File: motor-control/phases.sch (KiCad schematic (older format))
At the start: 39 parts

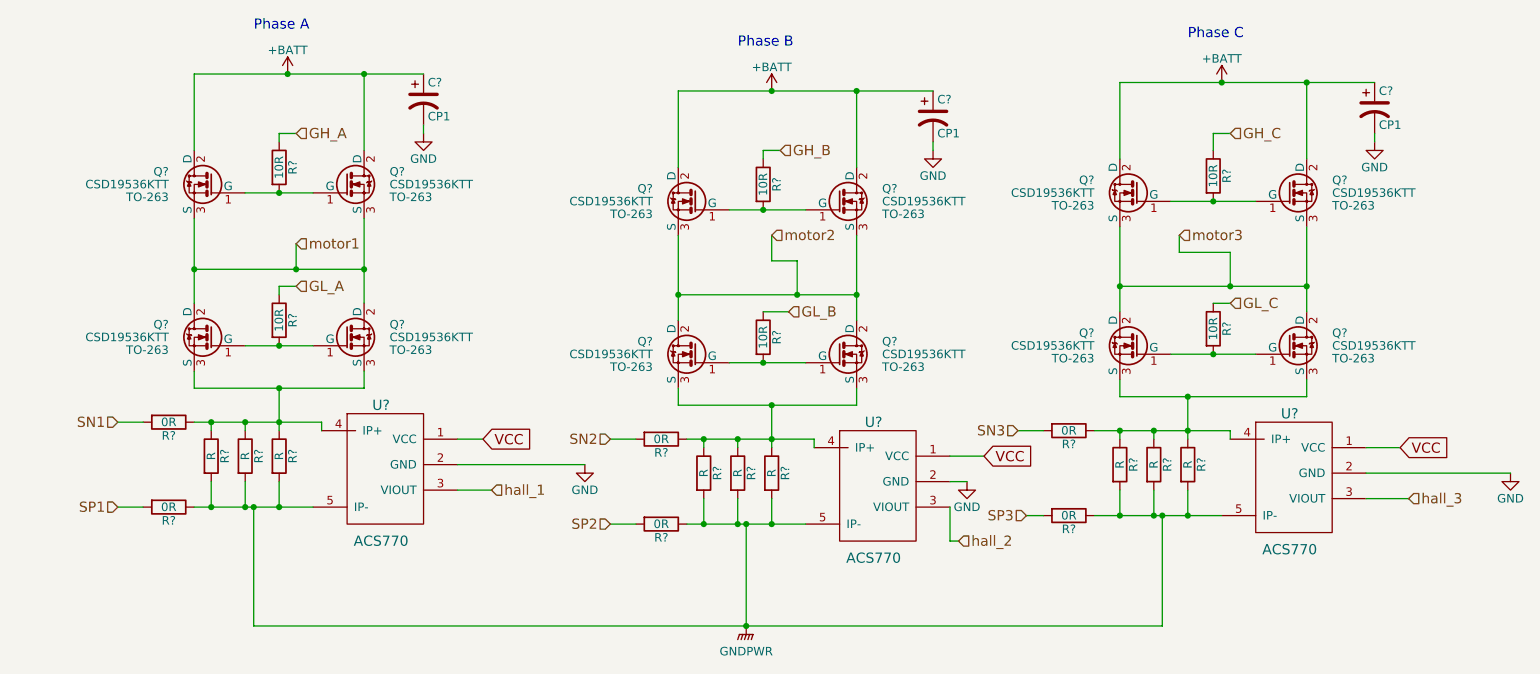
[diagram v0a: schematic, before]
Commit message: Almost finished gate driver schematic
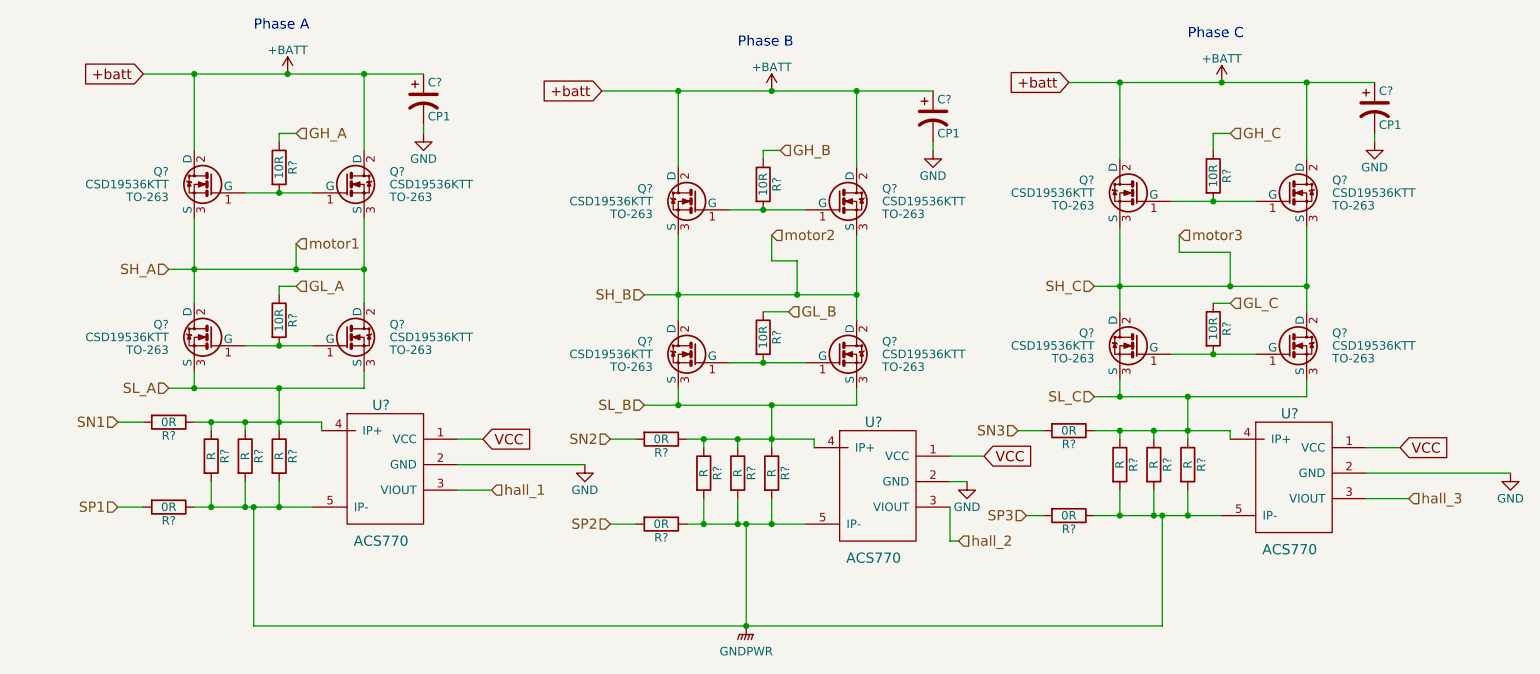
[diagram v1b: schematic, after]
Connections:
- net SL_A: now reaches Q?.3 (S), Q?.3 (S), R?.1, R?.1, R?.1, R?.1, U?.4 (IP+)
- net SL_B: now reaches Q?.3 (S), Q?.3 (S), R?.1, R?.1, R?.1, R?.1, U?.4 (IP+)
- net SL_C: now reaches Q?.3 (S), Q?.3 (S), R?.1, R?.1, R?.1, R?.1, U?.4 (IP+)
- net motor1 renamed SH_A
- net motor2 renamed SH_B
- net motor3 renamed SH_C
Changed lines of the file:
@@
 encoding utf-8
 Sheet 2 3
-Title ""
-Date ""
-Rev ""
-Comp ""
-Comment1 ""
+Title "Power MOSFETs"
+Date "2015-11-18"
+Rev "1"
+Comp "RIT Senior Design"
+Comment1 "Joseph Kubeck"
 Comment2 ""
 Comment3 ""
@@
 	4650 2300 4650 2250
 Wire Wire Line
-	3300 1950 4650 1950
+	3000 1950 4650 1950
 Wire Wire Line
 	4300 1950 4300 2400
@@
 	4300 3800 4300 3700
 Wire Wire Line
-	3300 3800 4300 3800
+	3150 3800 4300 3800
 Wire Wire Line
 	3300 3800 3300 3700
@@
 	3300 2800 3300 3300
 Wire Wire Line
-	3300 3100 4300 3100
+	3150 3100 4300 3100
 Connection ~ 4300 3100
 Connection ~ 3300 3100
@@
 $EndComp
 Wire Wire Line
-	6150 2050 7650 2050
+	5700 2050 7650 2050
 Wire Wire Line
 	7200 2050 7200 2500
@@
 	7200 3900 7200 3800
 Wire Wire Line
-	6150 3900 7200 3900
+	5950 3900 7200 3900
 Wire Wire Line
 	6150 3900 6150 3800
 Connection ~ 6700 3900
 Wire Wire Line
-	6150 3250 7200 3250
+	5950 3250 7200 3250
 Connection ~ 7200 3250
 Connection ~ 6150 3250
@@
 $EndComp
 Wire Wire Line
-	8750 2000 10250 2000
+	8450 2000 10250 2000
 Wire Wire Line
 	9850 2000 9850 2450
@@
 	8750 3750 8750 3850
 Wire Wire Line
-	8750 3850 9850 3850
+	8600 3850 9850 3850
 Wire Wire Line
 	9850 3850 9850 3750
 Wire Wire Line
-	8750 3200 9850 3200
+	8600 3200 9850 3200
 Connection ~ 9850 3200
 Connection ~ 8750 3200
@@
 Connection ~ 3400 4000
 Connection ~ 3400 4500
+Text HLabel 3150 3100 0    60   Input ~ 0
+SH_A
+Text HLabel 3150 3800 0    60   Input ~ 0
+SL_A
+Text HLabel 5950 3250 0    60   Input ~ 0
+SH_B
+Text HLabel 5950 3900 0    60   Input ~ 0
+SL_B
+Text HLabel 8600 3200 0    60   Input ~ 0
+SH_C
+Text HLabel 8600 3850 0    60   Input ~ 0
+SL_C
+Connection ~ 3300 3800
+Connection ~ 6150 3900
+Connection ~ 8750 3850
+Text GLabel 3000 1950 0    60   Input ~ 0
++batt
+Connection ~ 3300 1950
+Text GLabel 5700 2050 0    60   Input ~ 0
++batt
+Text GLabel 8450 2000 0    60   Input ~ 0
++batt
+Connection ~ 6150 2050
+Connection ~ 8750 2000
 $EndSCHEMATC

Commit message: Annotated schematic & matched footprints
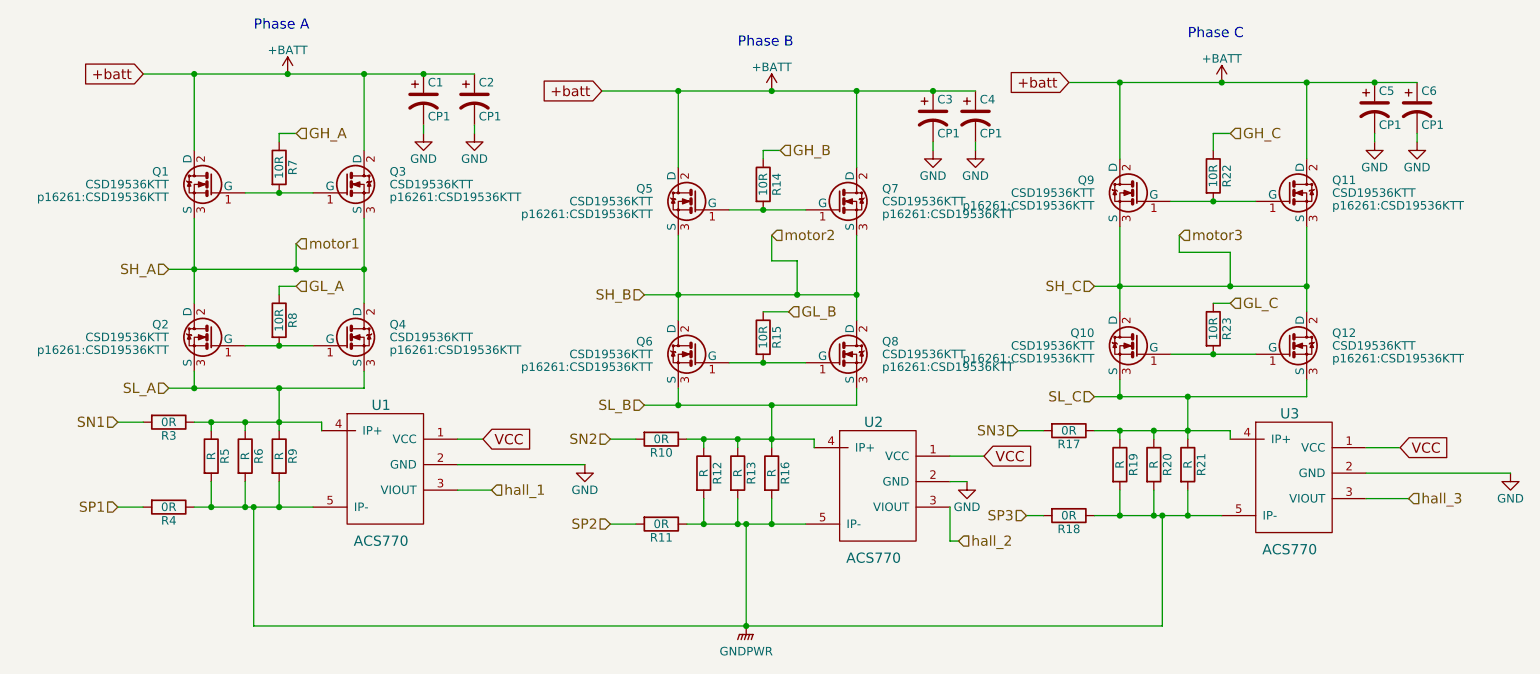
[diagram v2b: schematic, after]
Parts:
- added C2, C4, C6: CP1, Capacitors_Elko_ThroughHole:Elko_vert_31.5x16mm_RM7.5, symbol CP1
- C1, C3, C5: renamed from C?; footprint (none) -> Capacitors_Elko_ThroughHole:Elko_vert_31.5x16mm_RM7.5
- Q1, Q10, Q11, Q12, Q2, Q3, Q4, Q5, Q6, Q7, Q8, Q9: renamed from Q?; footprint TO-263 -> p16261:CSD19536KTT
- R10, R11, R12, R13, R14, R15, R16, R17, R18, R19, R20, R21, R22, R23, R3, R4, R5, R6, R7, R8, R9: renamed from R?; footprint (none) -> Resistors_SMD:R_0805
- U1, U2, U3: renamed from U?; footprint (none) -> p16261:ACS770xCB
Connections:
- net +BATT: now also C2.1, C4.1, C6.1
- net GND: now also C2.2, C4.2, C6.2

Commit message: started revision 2 of board, changed to thru fets
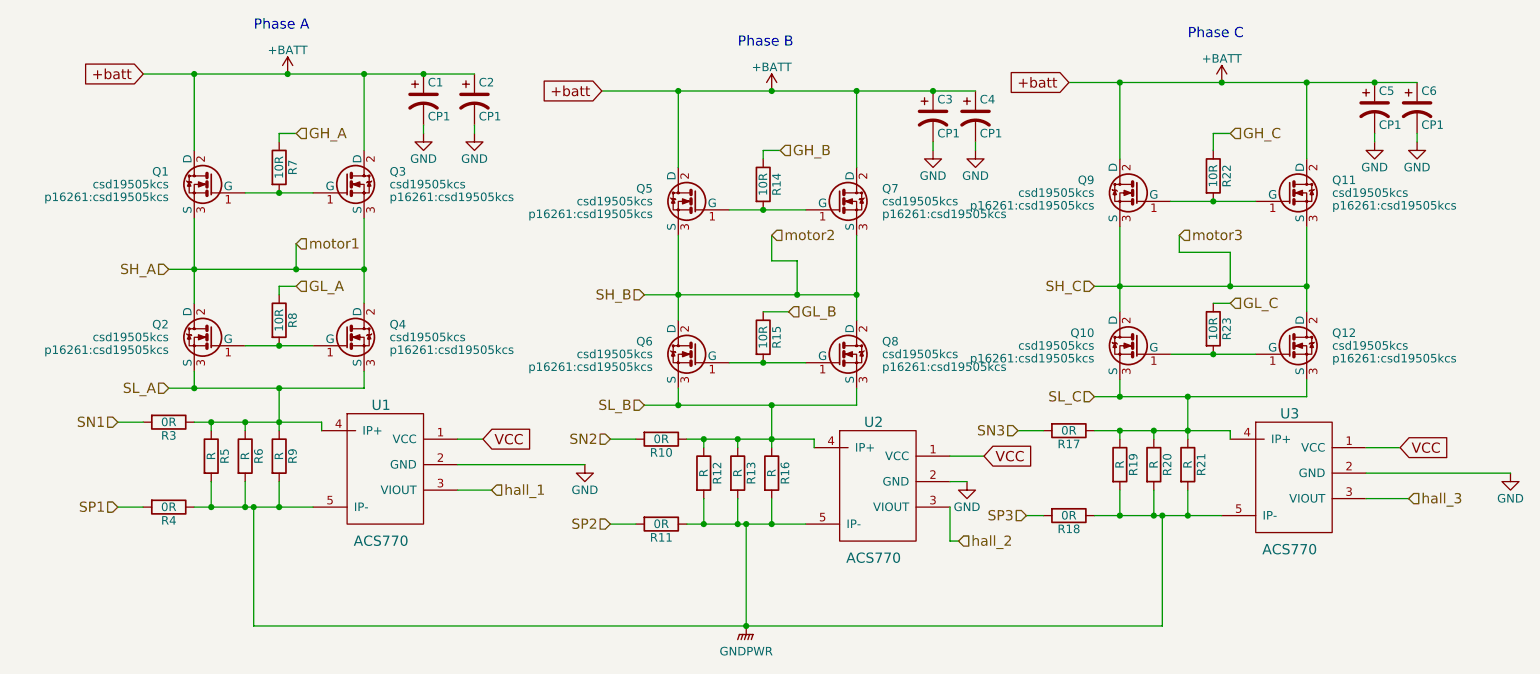
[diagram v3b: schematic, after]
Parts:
- Q1, Q10, Q11, Q12, Q2, Q3, Q4, Q5, Q6, Q7, Q8, Q9: value CSD19536KTT -> csd19505kcs; footprint p16261:CSD19536KTT -> p16261:csd19505kcs
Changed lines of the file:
@@
 P 3400 2600
 F 0 "Q1" H 3650 2675 50  0000 L CNN
-F 1 "CSD19536KTT" H 3650 2600 50  0000 L CNN
-F 2 "p16261:CSD19536KTT" H 3650 2525 50  0000 L CNN
+F 1 "csd19505kcs" H 3650 2600 50  0000 L CNN
+F 2 "p16261:csd19505kcs" H 3650 2525 50  0000 L CNN
 F 3 "" H 3400 2600 50  0000 L CNN
 	1    3400 2600
@@
 P 4200 2600
 F 0 "Q3" H 4450 2675 50  0000 L CNN
-F 1 "CSD19536KTT" H 4450 2600 50  0000 L CNN
-F 2 "p16261:CSD19536KTT" H 4450 2525 50  0000 L CNN
+F 1 "csd19505kcs" H 4450 2600 50  0000 L CNN
+F 2 "p16261:csd19505kcs" H 4450 2525 50  0000 L CNN
 F 3 "" H 4200 2600 50  0000 L CNN
 	1    4200 2600
@@
 P 3400 3500
 F 0 "Q2" H 3650 3575 50  0000 L CNN
-F 1 "CSD19536KTT" H 3650 3500 50  0000 L CNN
-F 2 "p16261:CSD19536KTT" H 3650 3425 50  0000 L CNN
+F 1 "csd19505kcs" H 3650 3500 50  0000 L CNN
+F 2 "p16261:csd19505kcs" H 3650 3425 50  0000 L CNN
 F 3 "" H 3400 3500 50  0000 L CNN
 	1    3400 3500
@@
 P 4200 3500
 F 0 "Q4" H 4450 3575 50  0000 L CNN
-F 1 "CSD19536KTT" H 4450 3500 50  0000 L CNN
-F 2 "p16261:CSD19536KTT" H 4450 3425 50  0000 L CNN
+F 1 "csd19505kcs" H 4450 3500 50  0000 L CNN
+F 2 "p16261:csd19505kcs" H 4450 3425 50  0000 L CNN
 F 3 "" H 4200 3500 50  0000 L CNN
 	1    4200 3500
@@
 P 6250 3600
 F 0 "Q6" H 6500 3675 50  0000 L CNN
-F 1 "CSD19536KTT" H 6500 3600 50  0000 L CNN
-F 2 "p16261:CSD19536KTT" H 6500 3525 50  0000 L CNN
+F 1 "csd19505kcs" H 6500 3600 50  0000 L CNN
+F 2 "p16261:csd19505kcs" H 6500 3525 50  0000 L CNN
 F 3 "" H 6250 3600 50  0000 L CNN
 	1    6250 3600
@@
 P 7100 3600
 F 0 "Q8" H 7350 3675 50  0000 L CNN
-F 1 "CSD19536KTT" H 7350 3600 50  0000 L CNN
-F 2 "p16261:CSD19536KTT" H 7350 3525 50  0000 L CNN
+F 1 "csd19505kcs" H 7350 3600 50  0000 L CNN
+F 2 "p16261:csd19505kcs" H 7350 3525 50  0000 L CNN
 F 3 "" H 7100 3600 50  0000 L CNN
 	1    7100 3600
@@
 P 6250 2700
 F 0 "Q5" H 6500 2775 50  0000 L CNN
-F 1 "CSD19536KTT" H 6500 2700 50  0000 L CNN
-F 2 "p16261:CSD19536KTT" H 6500 2625 50  0000 L CNN
+F 1 "csd19505kcs" H 6500 2700 50  0000 L CNN
+F 2 "p16261:csd19505kcs" H 6500 2625 50  0000 L CNN
 F 3 "" H 6250 2700 50  0000 L CNN
 	1    6250 2700
@@
 P 7100 2700
 F 0 "Q7" H 7350 2775 50  0000 L CNN
-F 1 "CSD19536KTT" H 7350 2700 50  0000 L CNN
-F 2 "p16261:CSD19536KTT" H 7350 2625 50  0000 L CNN
+F 1 "csd19505kcs" H 7350 2700 50  0000 L CNN
+F 2 "p16261:csd19505kcs" H 7350 2625 50  0000 L CNN
 F 3 "" H 7100 2700 50  0000 L CNN
 	1    7100 2700
@@
 P 8850 2650
 F 0 "Q9" H 9100 2725 50  0000 L CNN
-F 1 "CSD19536KTT" H 9100 2650 50  0000 L CNN
-F 2 "p16261:CSD19536KTT" H 9100 2575 50  0000 L CNN
+F 1 "csd19505kcs" H 9100 2650 50  0000 L CNN
+F 2 "p16261:csd19505kcs" H 9100 2575 50  0000 L CNN
 F 3 "" H 8850 2650 50  0000 L CNN
 	1    8850 2650
@@
 P 9750 2650
 F 0 "Q11" H 10000 2725 50  0000 L CNN
-F 1 "CSD19536KTT" H 10000 2650 50  0000 L CNN
-F 2 "p16261:CSD19536KTT" H 10000 2575 50  0000 L CNN
+F 1 "csd19505kcs" H 10000 2650 50  0000 L CNN
+F 2 "p16261:csd19505kcs" H 10000 2575 50  0000 L CNN
 F 3 "" H 9750 2650 50  0000 L CNN
 	1    9750 2650
@@
 P 8850 3550
 F 0 "Q10" H 9100 3625 50  0000 L CNN
-F 1 "CSD19536KTT" H 9100 3550 50  0000 L CNN
-F 2 "p16261:CSD19536KTT" H 9100 3475 50  0000 L CNN
+F 1 "csd19505kcs" H 9100 3550 50  0000 L CNN
+F 2 "p16261:csd19505kcs" H 9100 3475 50  0000 L CNN
 F 3 "" H 8850 3550 50  0000 L CNN
 	1    8850 3550
@@
 P 9750 3550
 F 0 "Q12" H 10000 3625 50  0000 L CNN
-F 1 "CSD19536KTT" H 10000 3550 50  0000 L CNN
-F 2 "p16261:CSD19536KTT" H 10000 3475 50  0000 L CNN
+F 1 "csd19505kcs" H 10000 3550 50  0000 L CNN
+F 2 "p16261:csd19505kcs" H 10000 3475 50  0000 L CNN
 F 3 "" H 9750 3550 50  0000 L CNN
 	1    9750 3550

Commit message: Just trying to get things together
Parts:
- C1, C2, C3, C4, C5, C6: footprint Capacitors_Elko_ThroughHole:Elko_vert_31.5x16mm_RM7.5 -> Capacitors_ThroughHole:C_Radial_D16_L30_P7.5
- R12, R13, R16, R19, R20, R21, R5, R6, R9: footprint Resistors_SMD:R_0805 -> Resistors_ThroughHole:Resistor_Vertical_RM7.5mm
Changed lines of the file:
@@
 F 0 "C1" H 4675 2200 50  0000 L CNN
 F 1 "CP1" H 4675 2000 50  0000 L CNN
-F 2 "Capacitors_Elko_ThroughHole:Elko_vert_31.5x16mm_RM7.5" H 4650 2100 60  0001 C CNN
+F 2 "Capacitors_ThroughHole:C_Radial_D16_L30_P7.5" H 4650 2100 60  0001 C CNN
 F 3 "" H 4650 2100 60  0000 C CNN
 	1    4650 2100
@@
 F 0 "Q1" H 3650 2675 50  0000 L CNN
 F 1 "csd19505kcs" H 3650 2600 50  0000 L CNN
-F 2 "p16261:csd19505kcs" H 3650 2525 50  0000 L CNN
+F 2 "p16261:csd19505kcs" H 3650 2525 50  0001 L CNN
 F 3 "" H 3400 2600 50  0000 L CNN
 	1    3400 2600
@@
 F 0 "Q3" H 4450 2675 50  0000 L CNN
 F 1 "csd19505kcs" H 4450 2600 50  0000 L CNN
-F 2 "p16261:csd19505kcs" H 4450 2525 50  0000 L CNN
+F 2 "p16261:csd19505kcs" H 4450 2525 50  0001 L CNN
 F 3 "" H 4200 2600 50  0000 L CNN
 	1    4200 2600
@@
 F 0 "Q2" H 3650 3575 50  0000 L CNN
 F 1 "csd19505kcs" H 3650 3500 50  0000 L CNN
-F 2 "p16261:csd19505kcs" H 3650 3425 50  0000 L CNN
+F 2 "p16261:csd19505kcs" H 3650 3425 50  0001 L CNN
 F 3 "" H 3400 3500 50  0000 L CNN
 	1    3400 3500
@@
 F 0 "Q4" H 4450 3575 50  0000 L CNN
 F 1 "csd19505kcs" H 4450 3500 50  0000 L CNN
-F 2 "p16261:csd19505kcs" H 4450 3425 50  0000 L CNN
+F 2 "p16261:csd19505kcs" H 4450 3425 50  0001 L CNN
 F 3 "" H 4200 3500 50  0000 L CNN
 	1    4200 3500
@@
 F 0 "R9" V 3880 4200 50  0000 C CNN
 F 1 "R" V 3800 4200 50  0000 C CNN
-F 2 "Resistors_SMD:R_0805" V 3730 4200 30  0001 C CNN
+F 2 "Resistors_ThroughHole:Resistor_Vertical_RM7.5mm" V 3730 4200 30  0001 C CNN
 F 3 "" H 3800 4200 30  0000 C CNN
 	1    3800 4200
@@
 F 0 "R6" V 3680 4200 50  0000 C CNN
 F 1 "R" V 3600 4200 50  0000 C CNN
-F 2 "Resistors_SMD:R_0805" V 3530 4200 30  0001 C CNN
+F 2 "Resistors_ThroughHole:Resistor_Vertical_RM7.5mm" V 3530 4200 30  0001 C CNN
 F 3 "" H 3600 4200 30  0000 C CNN
 	1    3600 4200
@@
 F 0 "R5" V 3480 4200 50  0000 C CNN
 F 1 "R" V 3400 4200 50  0000 C CNN
-F 2 "Resistors_SMD:R_0805" V 3330 4200 30  0001 C CNN
+F 2 "Resistors_ThroughHole:Resistor_Vertical_RM7.5mm" V 3330 4200 30  0001 C CNN
 F 3 "" H 3400 4200 30  0000 C CNN
 	1    3400 4200
@@
 F 0 "C3" H 7675 2300 50  0000 L CNN
 F 1 "CP1" H 7675 2100 50  0000 L CNN
-F 2 "Capacitors_Elko_ThroughHole:Elko_vert_31.5x16mm_RM7.5" H 7650 2200 60  0001 C CNN
+F 2 "Capacitors_ThroughHole:C_Radial_D16_L30_P7.5" H 7650 2200 60  0001 C CNN
 F 3 "" H 7650 2200 60  0000 C CNN
 	1    7650 2200
@@
 F 0 "Q6" H 6500 3675 50  0000 L CNN
 F 1 "csd19505kcs" H 6500 3600 50  0000 L CNN
-F 2 "p16261:csd19505kcs" H 6500 3525 50  0000 L CNN
+F 2 "p16261:csd19505kcs" H 6500 3525 50  0001 L CNN
 F 3 "" H 6250 3600 50  0000 L CNN
 	1    6250 3600
@@
 F 0 "Q8" H 7350 3675 50  0000 L CNN
 F 1 "csd19505kcs" H 7350 3600 50  0000 L CNN
-F 2 "p16261:csd19505kcs" H 7350 3525 50  0000 L CNN
+F 2 "p16261:csd19505kcs" H 7350 3525 50  0001 L CNN
 F 3 "" H 7100 3600 50  0000 L CNN
 	1    7100 3600
@@
 F 0 "Q5" H 6500 2775 50  0000 L CNN
 F 1 "csd19505kcs" H 6500 2700 50  0000 L CNN
-F 2 "p16261:csd19505kcs" H 6500 2625 50  0000 L CNN
+F 2 "p16261:csd19505kcs" H 6500 2625 50  0001 L CNN
 F 3 "" H 6250 2700 50  0000 L CNN
 	1    6250 2700
@@
 F 0 "Q7" H 7350 2775 50  0000 L CNN
 F 1 "csd19505kcs" H 7350 2700 50  0000 L CNN
-F 2 "p16261:csd19505kcs" H 7350 2625 50  0000 L CNN
+F 2 "p16261:csd19505kcs" H 7350 2625 50  0001 L CNN
 F 3 "" H 7100 2700 50  0000 L CNN
 	1    7100 2700
@@
 F 0 "R12" V 6380 4300 50  0000 C CNN
 F 1 "R" V 6300 4300 50  0000 C CNN
-F 2 "Resistors_SMD:R_0805" V 6230 4300 30  0001 C CNN
+F 2 "Resistors_ThroughHole:Resistor_Vertical_RM7.5mm" V 6230 4300 30  0001 C CNN
 F 3 "" H 6300 4300 30  0000 C CNN
 	1    6300 4300
@@
 F 0 "R13" V 6580 4300 50  0000 C CNN
 F 1 "R" V 6500 4300 50  0000 C CNN
-F 2 "Resistors_SMD:R_0805" V 6430 4300 30  0001 C CNN
+F 2 "Resistors_ThroughHole:Resistor_Vertical_RM7.5mm" V 6430 4300 30  0001 C CNN
 F 3 "" H 6500 4300 30  0000 C CNN
 	1    6500 4300
@@
 F 0 "R16" V 6780 4300 50  0000 C CNN
 F 1 "R" V 6700 4300 50  0000 C CNN
-F 2 "Resistors_SMD:R_0805" V 6630 4300 30  0001 C CNN
+F 2 "Resistors_ThroughHole:Resistor_Vertical_RM7.5mm" V 6630 4300 30  0001 C CNN
 F 3 "" H 6700 4300 30  0000 C CNN
 	1    6700 4300
@@
 F 0 "Q9" H 9100 2725 50  0000 L CNN
 F 1 "csd19505kcs" H 9100 2650 50  0000 L CNN
-F 2 "p16261:csd19505kcs" H 9100 2575 50  0000 L CNN
+F 2 "p16261:csd19505kcs" H 9100 2575 50  0001 L CNN
 F 3 "" H 8850 2650 50  0000 L CNN
 	1    8850 2650
@@
 F 0 "Q11" H 10000 2725 50  0000 L CNN
 F 1 "csd19505kcs" H 10000 2650 50  0000 L CNN
-F 2 "p16261:csd19505kcs" H 10000 2575 50  0000 L CNN
+F 2 "p16261:csd19505kcs" H 10000 2575 50  0001 L CNN
 F 3 "" H 9750 2650 50  0000 L CNN
 	1    9750 2650
@@
 F 0 "Q10" H 9100 3625 50  0000 L CNN
 F 1 "csd19505kcs" H 9100 3550 50  0000 L CNN
-F 2 "p16261:csd19505kcs" H 9100 3475 50  0000 L CNN
+F 2 "p16261:csd19505kcs" H 9100 3475 50  0001 L CNN
 F 3 "" H 8850 3550 50  0000 L CNN
 	1    8850 3550
@@
 F 0 "Q12" H 10000 3625 50  0000 L CNN
 F 1 "csd19505kcs" H 10000 3550 50  0000 L CNN
-F 2 "p16261:csd19505kcs" H 10000 3475 50  0000 L CNN
+F 2 "p16261:csd19505kcs" H 10000 3475 50  0001 L CNN
 F 3 "" H 9750 3550 50  0000 L CNN
 	1    9750 3550
@@
 F 0 "C5" H 10275 2250 50  0000 L CNN
 F 1 "CP1" H 10275 2050 50  0000 L CNN
-F 2 "Capacitors_Elko_ThroughHole:Elko_vert_31.5x16mm_RM7.5" H 10250 2150 60  0001 C CNN
+F 2 "Capacitors_ThroughHole:C_Radial_D16_L30_P7.5" H 10250 2150 60  0001 C CNN
 F 3 "" H 10250 2150 60  0000 C CNN
 	1    10250 2150
@@
 F 0 "R19" V 8830 4250 50  0000 C CNN
 F 1 "R" V 8750 4250 50  0000 C CNN
-F 2 "Resistors_SMD:R_0805" V 8680 4250 30  0001 C CNN
+F 2 "Resistors_ThroughHole:Resistor_Vertical_RM7.5mm" V 8680 4250 30  0001 C CNN
 F 3 "" H 8750 4250 30  0000 C CNN
 	1    8750 4250
@@
 F 0 "R20" V 9030 4250 50  0000 C CNN
 F 1 "R" V 8950 4250 50  0000 C CNN
-F 2 "Resistors_SMD:R_0805" V 8880 4250 30  0001 C CNN
+F 2 "Resistors_ThroughHole:Resistor_Vertical_RM7.5mm" V 8880 4250 30  0001 C CNN
 F 3 "" H 8950 4250 30  0000 C CNN
 	1    8950 4250
@@
 F 0 "R21" V 9230 4250 50  0000 C CNN
 F 1 "R" V 9150 4250 50  0000 C CNN
-F 2 "Resistors_SMD:R_0805" V 9080 4250 30  0001 C CNN
+F 2 "Resistors_ThroughHole:Resistor_Vertical_RM7.5mm" V 9080 4250 30  0001 C CNN
 F 3 "" H 9150 4250 30  0000 C CNN
 	1    9150 4250
@@
 F 0 "C2" H 4975 2200 50  0000 L CNN
 F 1 "CP1" H 4975 2000 50  0000 L CNN
-F 2 "Capacitors_Elko_ThroughHole:Elko_vert_31.5x16mm_RM7.5" H 4950 2100 60  0001 C CNN
+F 2 "Capacitors_ThroughHole:C_Radial_D16_L30_P7.5" H 4950 2100 60  0001 C CNN
 F 3 "" H 4950 2100 60  0000 C CNN
 	1    4950 2100
@@
 F 0 "C4" H 7925 2300 50  0000 L CNN
 F 1 "CP1" H 7925 2100 50  0000 L CNN
-F 2 "Capacitors_Elko_ThroughHole:Elko_vert_31.5x16mm_RM7.5" H 7900 2200 60  0001 C CNN
+F 2 "Capacitors_ThroughHole:C_Radial_D16_L30_P7.5" H 7900 2200 60  0001 C CNN
 F 3 "" H 7900 2200 60  0000 C CNN
 	1    7900 2200
@@
 F 0 "C6" H 10525 2250 50  0000 L CNN
 F 1 "CP1" H 10525 2050 50  0000 L CNN
-F 2 "Capacitors_Elko_ThroughHole:Elko_vert_31.5x16mm_RM7.5" H 10500 2150 60  0001 C CNN
+F 2 "Capacitors_ThroughHole:C_Radial_D16_L30_P7.5" H 10500 2150 60  0001 C CNN
 F 3 "" H 10500 2150 60  0000 C CNN
 	1    10500 2150
